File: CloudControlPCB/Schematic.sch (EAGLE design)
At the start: 6 parts, among them J1 AUDIO_JACK_TRRSSMD_RA, U1 LPC4088FBD208, U2 SGTL5000XNLA3R2

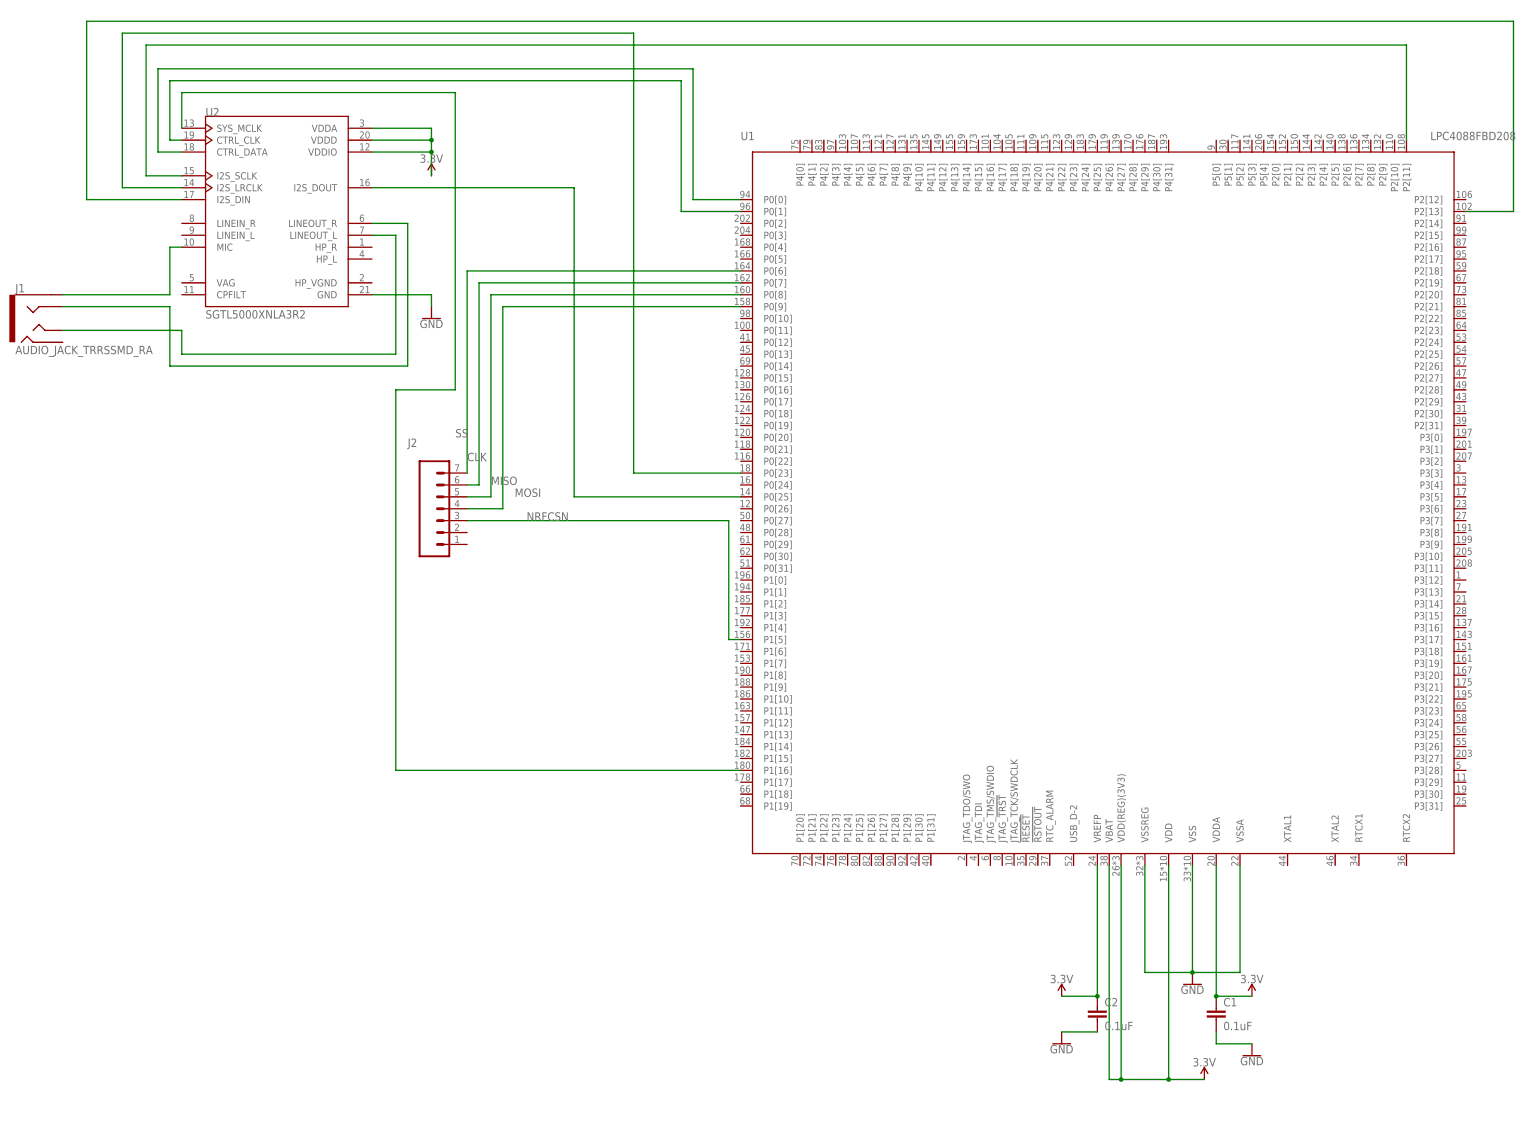
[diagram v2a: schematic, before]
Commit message: added more wireing
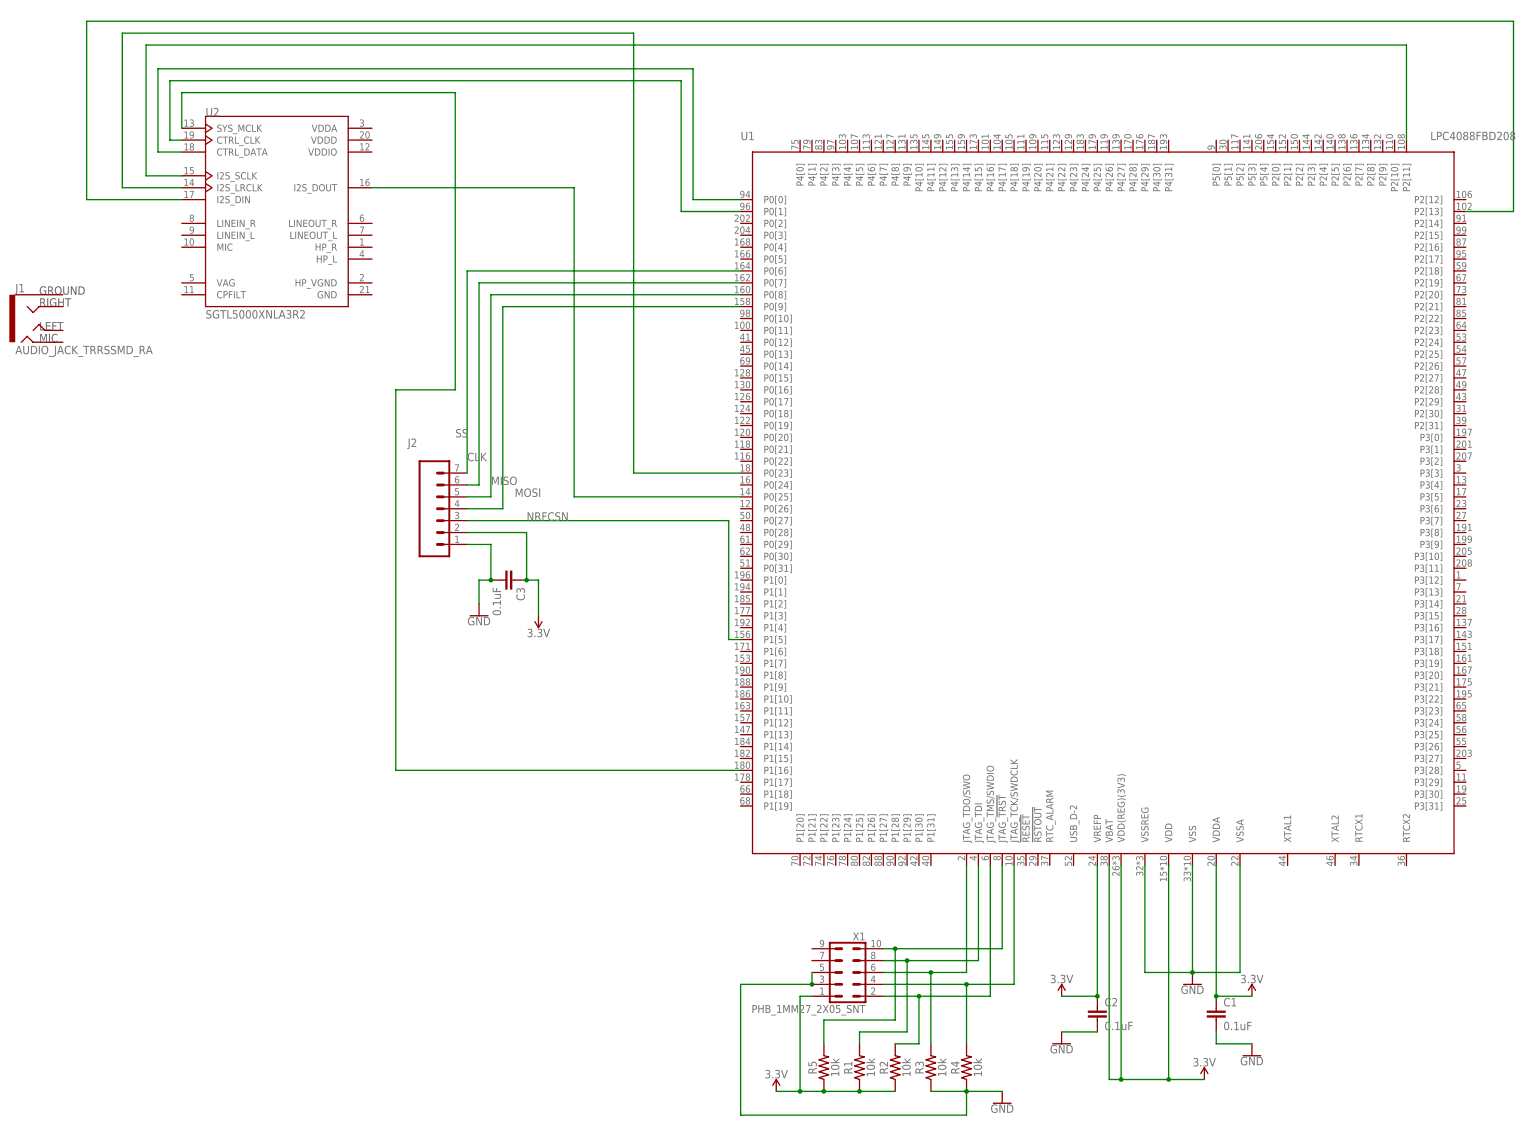
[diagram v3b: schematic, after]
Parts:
- added C3: 0.1uF, Homework1:0.1UF-0603-25V-(+80/-20%)
- added R1, R2, R3, R4, R5: 10k, Homework1:33OHM-0603-1/10W-1%
- added X1: PHB_1MM27_2X05_SNT, _hhn_con_pinhead_box_1mm27:PHB_1MM27_2X05_SNT
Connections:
- removed net N$1: J1.EARTH, U2.MIC
- removed net N$2: J1.RING1, U2.LINEOUT_R
- removed net N$3: J1.TIP, U2.LINEOUT_L
- new net N$12: R1.2, U1.JTAG_TDI, X1.8
- new net N$13: R2.2, U1.JTAG_TMS/SWDIO, X1.2
- new net N$14: R4.2, U1.JTAG_TCK/SWDCLK, X1.4
- new net N$16: R5.2, U1.JTAG_!TRST, X1.10
- new net N$9: R3.2, U1.JTAG_TDO/SWO, X1.6
- net 3.3V: now also C3.1, J2.2, R1.1, R2.1, R5.1, X1.1; no longer U2.VDDA, U2.VDDD, U2.VDDIO
- net GND: now also C3.2, J2.1, R3.1, R4.1, X1.3, X1.5; no longer U2.GND
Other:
- note added: "GROUND"
- note added: "LEFT"
- note added: "MIC"
- note added: "RIGHT"

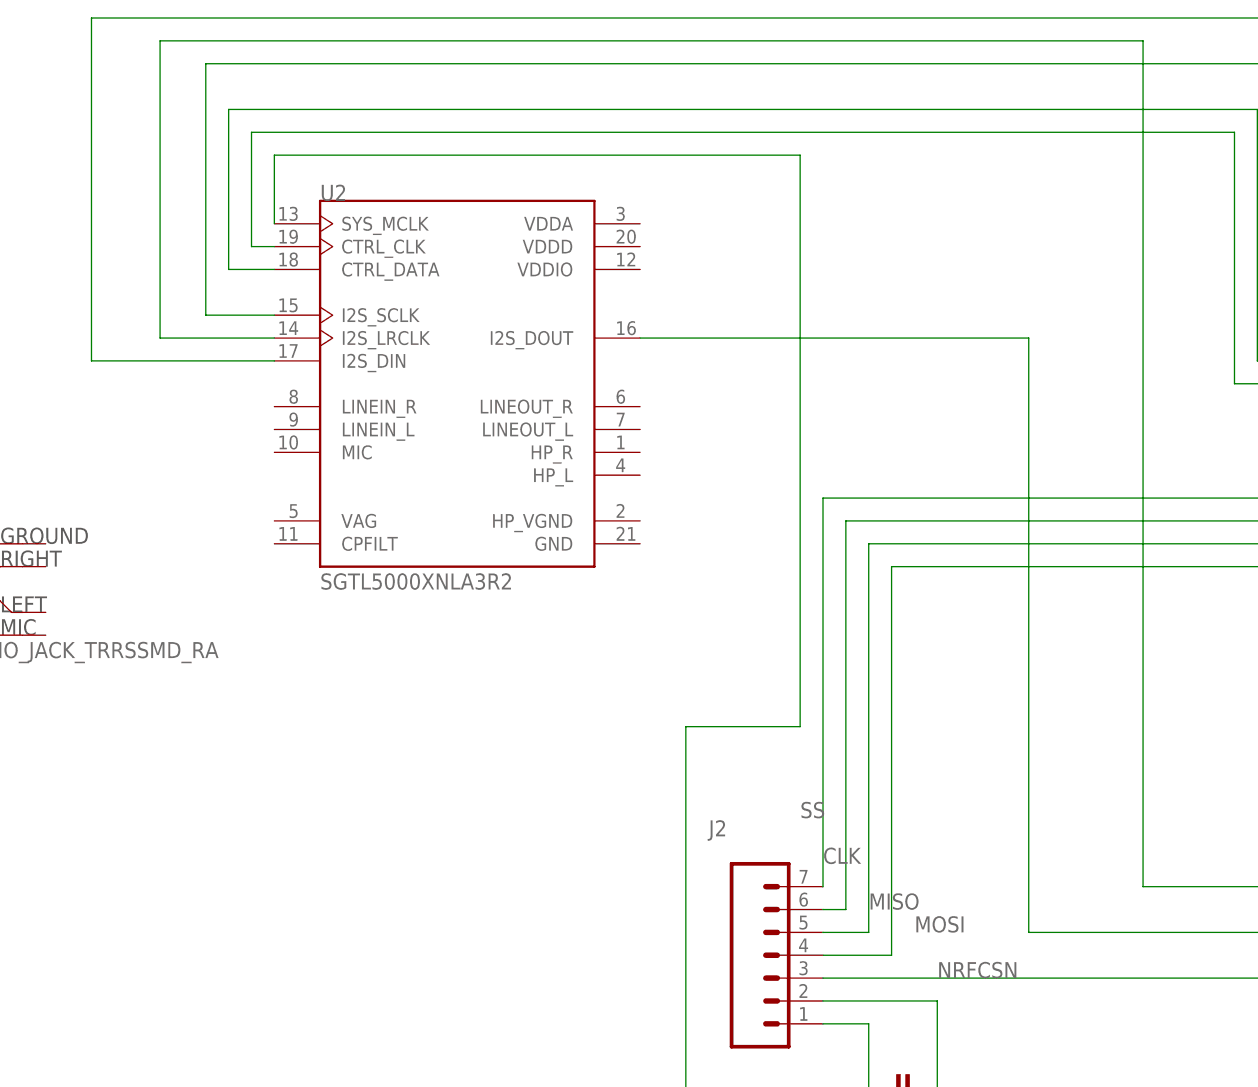
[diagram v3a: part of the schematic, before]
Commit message: Added codec capacitors into schematic, can't do much else without the amplifier module.
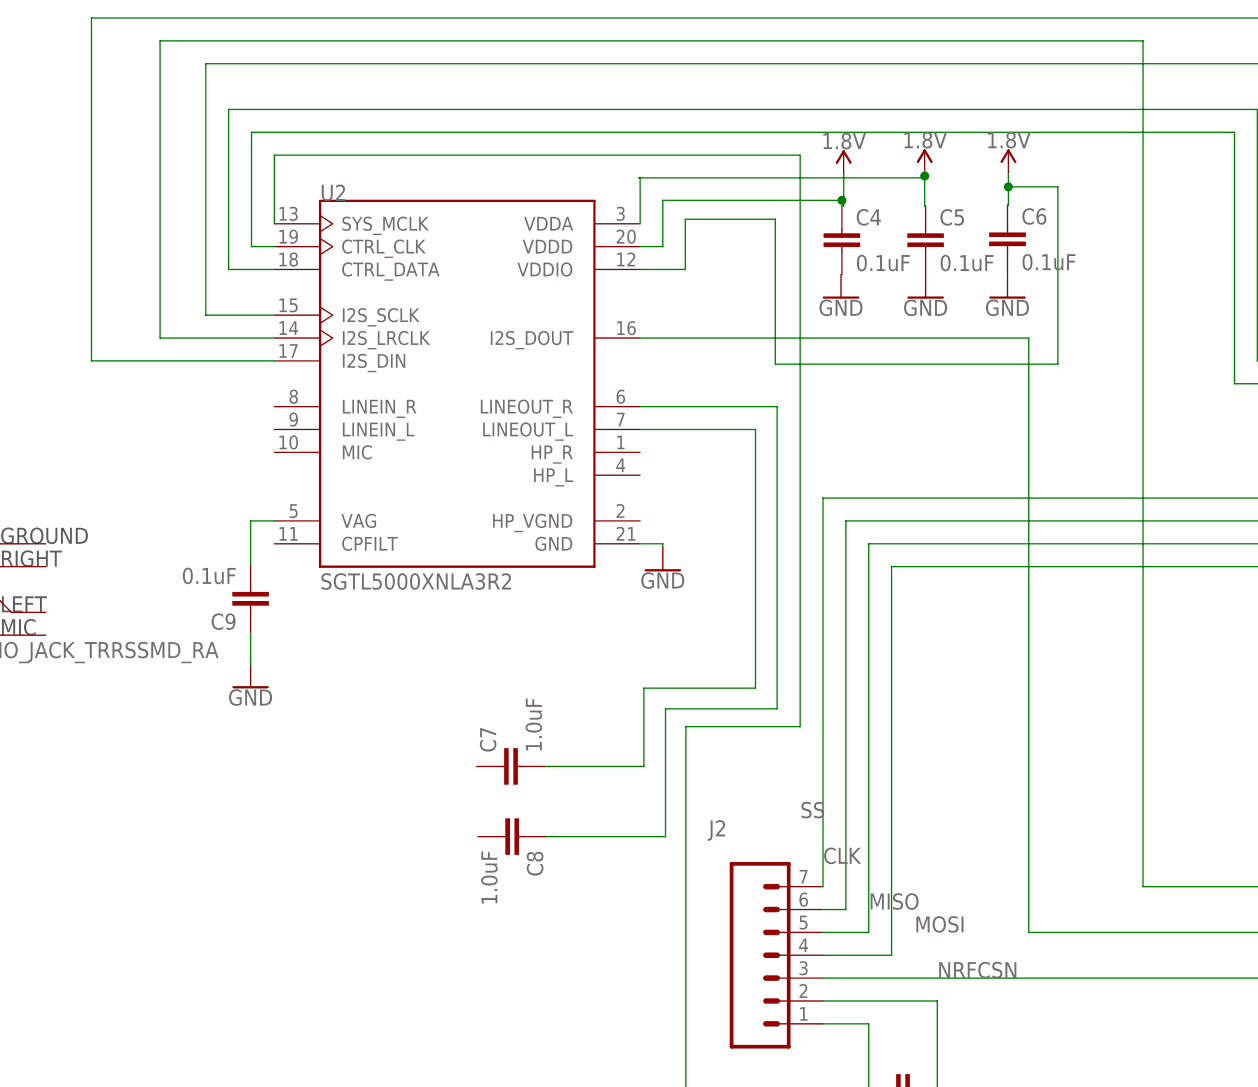
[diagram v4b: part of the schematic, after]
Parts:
- added C4, C5, C6, C9: 0.1uF, Homework1:0.1UF-0402-16V-10%
- added C7, C8: 1.0uF, Homework1:1.0UF-0402-16V-10%
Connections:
- new net 1.8V: C4.1, C5.1, C6.1, U2.VDDA, U2.VDDIO
- new net N$1: C8.1, U2.LINEOUT_R
- new net N$15: C9.2, U2.VAG
- new net N$2: C7.2, U2.LINEOUT_L
- new net N$3: U2.VDDD
- net GND: now also C9.1, U2.GND

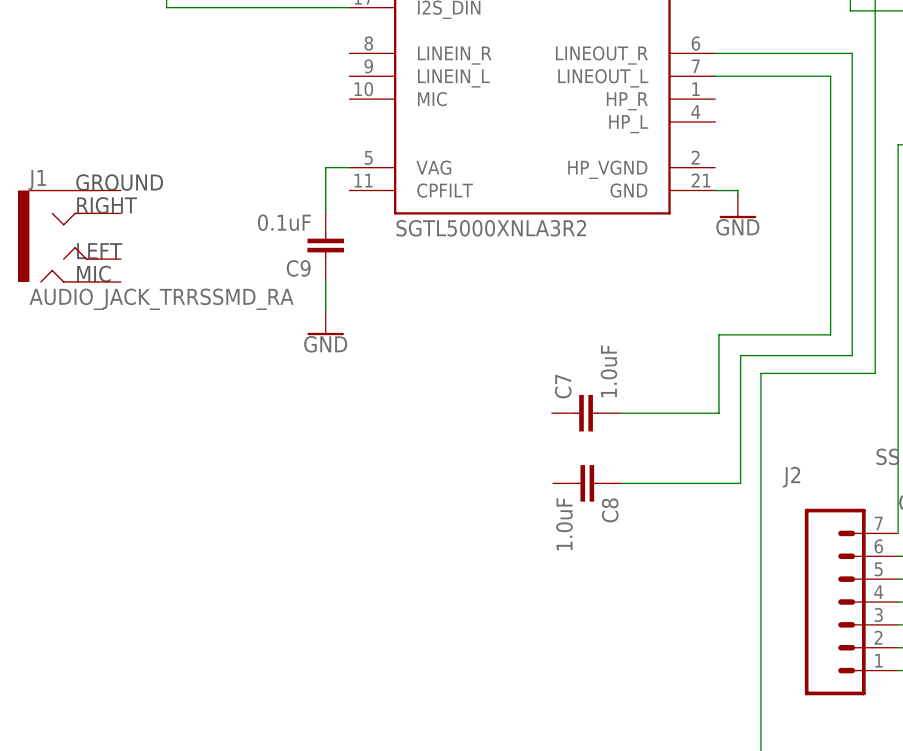
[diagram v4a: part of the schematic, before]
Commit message: fixed headphone jack
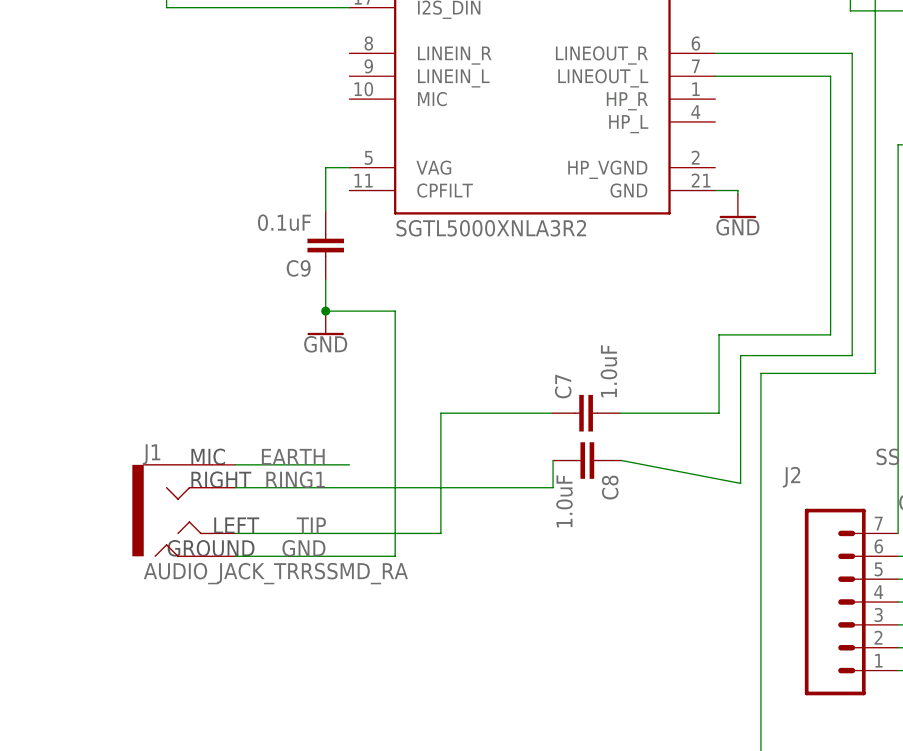
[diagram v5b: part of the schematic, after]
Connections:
- new net EARTH: J1.EARTH
- new net RING1: C8.2, J1.RING1
- new net TIP: C7.1, J1.TIP
- net GND: now also J1.RING2
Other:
- moved on the sheet: C8, J1
